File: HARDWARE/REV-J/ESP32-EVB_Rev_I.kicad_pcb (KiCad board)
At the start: 2 copper layers, 75.2 x 74.7 mm, 159 parts, among them CON1 TB3 DG306-5.0-3P, CON2 TB3 DG306-5.0-3P, Q1 BC817-40(SOT23), Q2 BC817-40(SOT23), Q3 Q12MHz/20pF/30ppm/2P/HC-49SM(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, Q4 BC817-40(SOT23), Q5 BC817-40(SOT23), Q6 BC817, Q7 BC817-40(SOT23), U1 BL4054B-42TPRN(SOT23-5), U10 BAT54C(SOT23-3), U2 SY8089AAAC(SOT23-5), U3 ESP-WROOM-32, U4 LAN8710A-EZC(QFN32), U5 CH340T(SSOP20W), U6 MCP2562-E/SN(SOIC-8_150mil), U7 RPM7236-H8, U8 NCP303LSN27T1G(SOT-23-5), U9 BAT54C(SOT23-3)

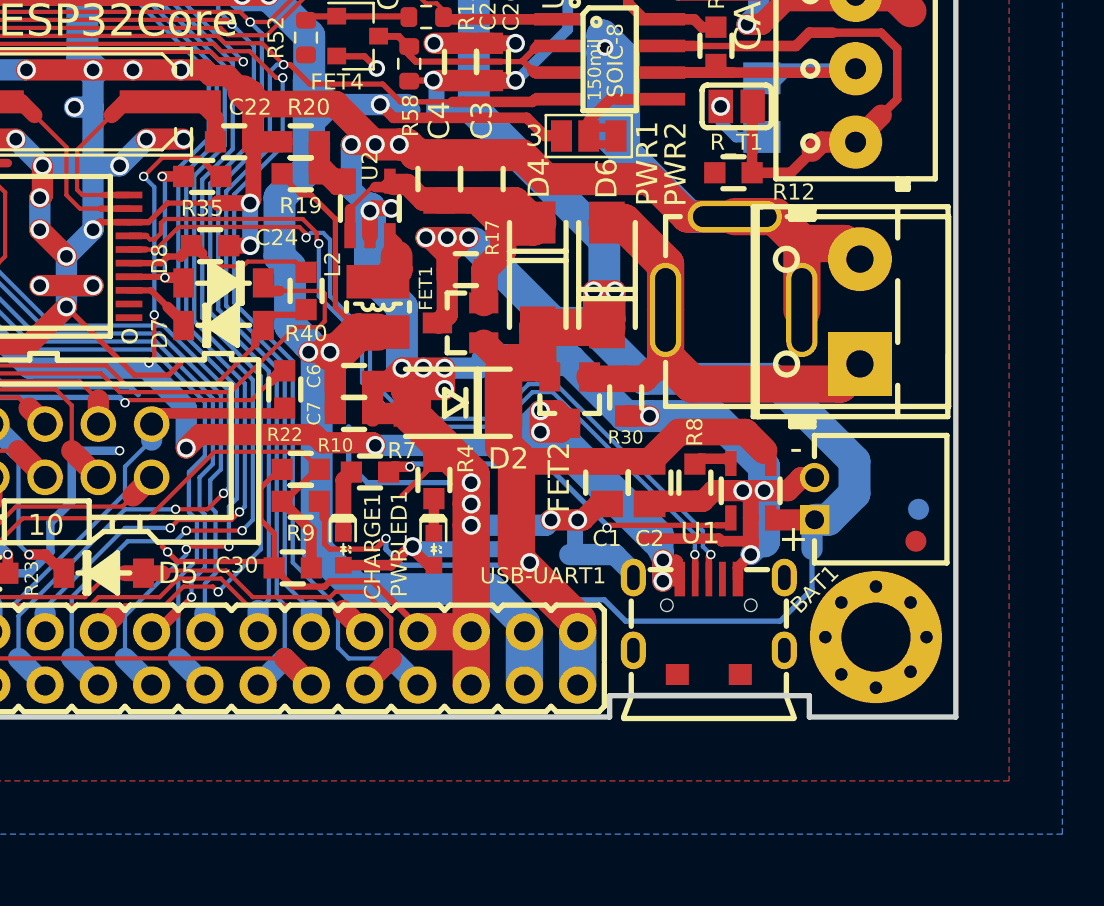
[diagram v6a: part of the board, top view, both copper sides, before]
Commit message: re-position usb port+bat conector
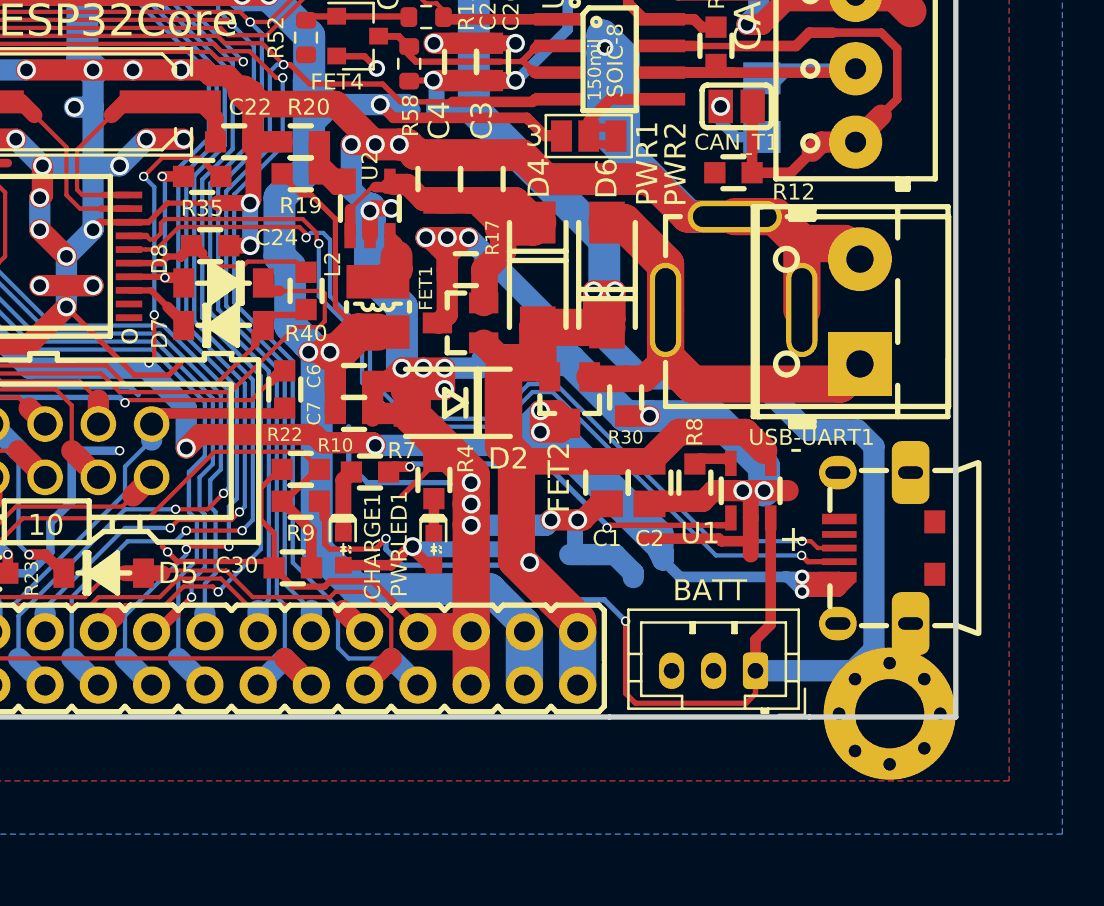
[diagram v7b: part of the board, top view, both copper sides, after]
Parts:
- removed BAT1: DW02R, OLIMEX_Connectors-FP:LIPO_BAT-CON2DW02R
- removed Fid2: , OLIMEX_Other-FP:Fiducial1x3
- removed GND1: TESTPAD, OLIMEX_Other-FP:TESTPAD_40-ROUND
- added BATT: Conn_01x03, Connector_JST:JST_PH_B3B-PH-K_1x03_P2.00mm_Vertical, F.Cu at (135.2, 139.5)
- moved USB-UART1 10.5 mm to (142.4, 133.7), turned to 0 degrees
- moved MH2 3.71 mm to (141.6, 141.6)
- renumbered R_T1 to CAN_T1
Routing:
- net /+5V_USB: track 86.5 -> 101.8 mm
- net Net-(FET1-Pad3): track 73.9 -> 88.7 mm, vias 4 -> 5
- net GND: track 1017.3 -> 1011.1 mm, vias 134 -> 133
- net Net-(U5-Pad7): track 40.4 -> 45.7 mm
- net Net-(U5-Pad6): track 40.8 -> 45.1 mm
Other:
- outline, holes or cut-outs redrawn

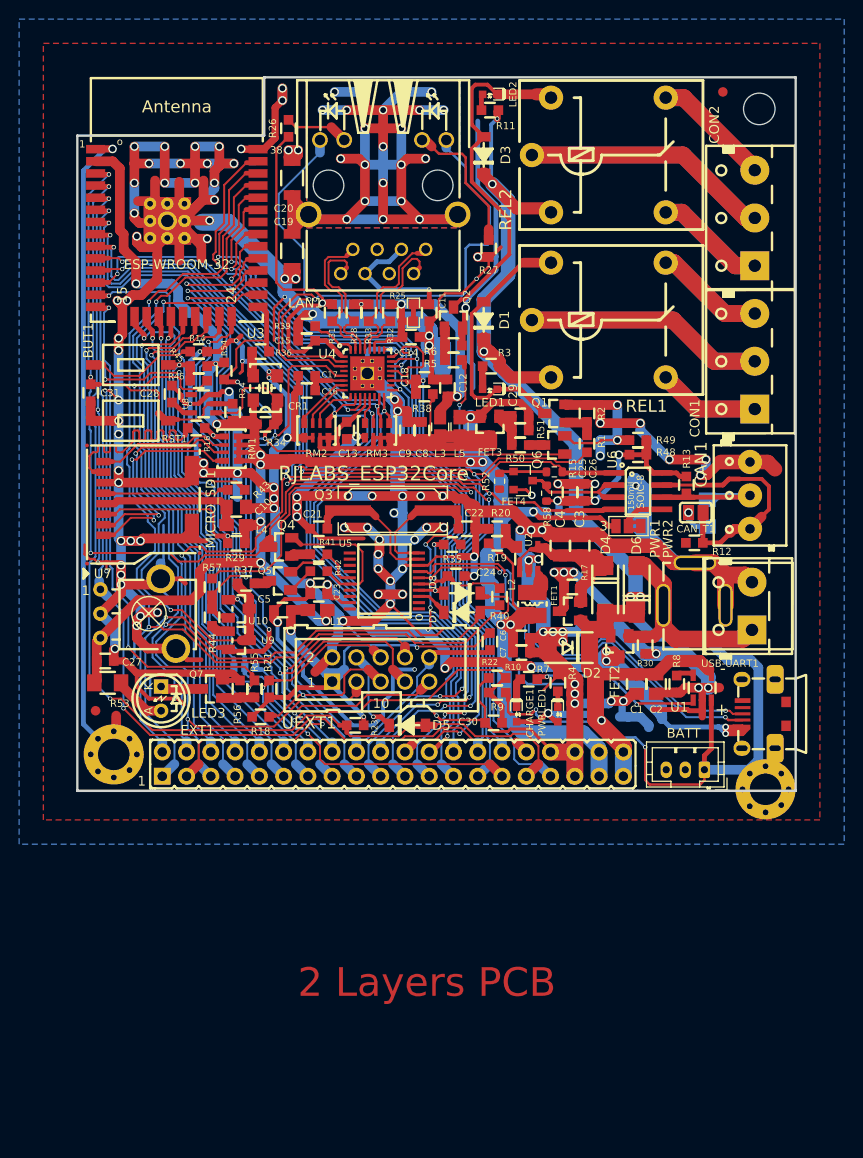
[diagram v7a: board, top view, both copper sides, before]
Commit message: done add 5 extension UEXT
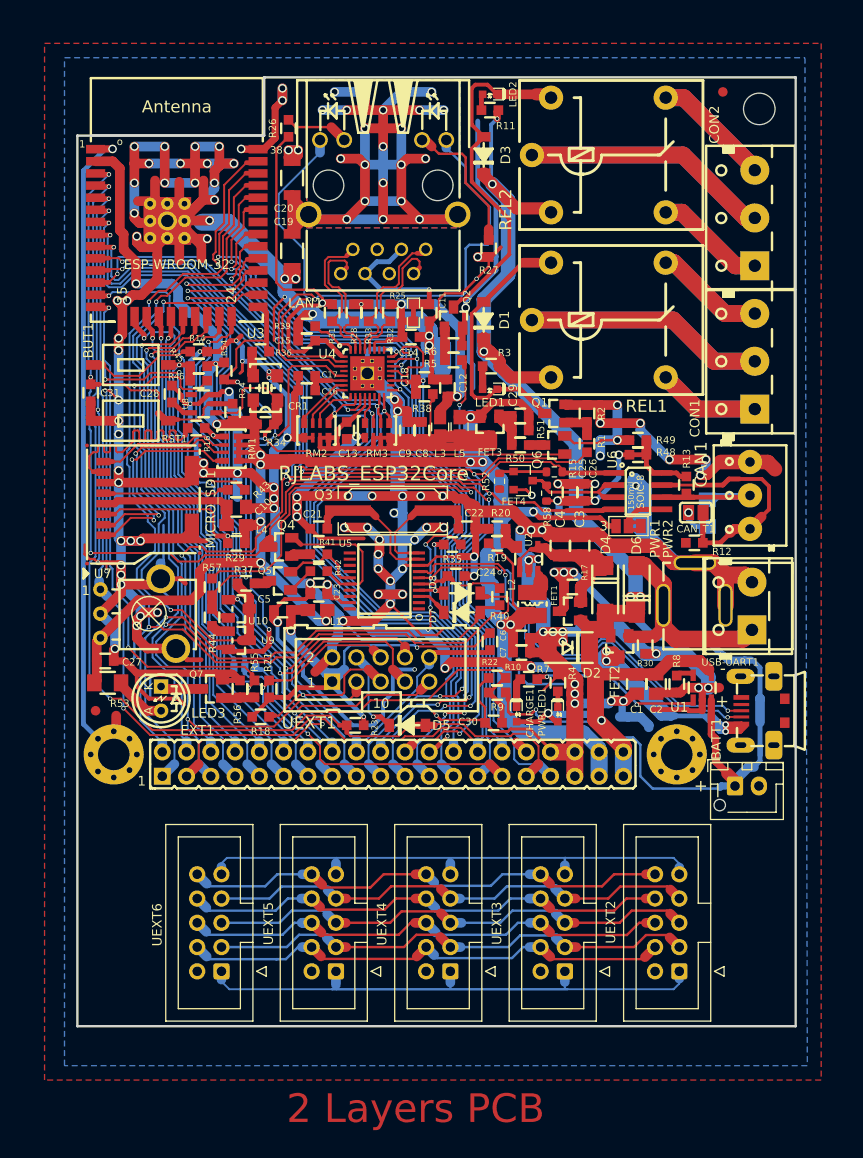
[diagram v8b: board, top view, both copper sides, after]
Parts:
- removed BATT: Conn_01x03, Connector_JST:JST_PH_B3B-PH-K_1x03_P2.00mm_Vertical
- added BATT1: Conn_01x02, Connector_JST:JST_XH_B2B-XH-AM_1x02_P2.50mm_Vertical, F.Cu at (138.4, 141.2)
- added UEXT2: BH10S, Connector_IDC:IDC-Header_2x05_P2.54mm_Vertical, F.Cu at (132.6, 160.6)
- added UEXT3: BH10S, Connector_IDC:IDC-Header_2x05_P2.54mm_Vertical, F.Cu at (120.6, 160.6)
- added UEXT4: BH10S, Connector_IDC:IDC-Header_2x05_P2.54mm_Vertical, F.Cu at (108.6, 160.6)
- added UEXT5: BH10S, Connector_IDC:IDC-Header_2x05_P2.54mm_Vertical, F.Cu at (96.7, 160.6)
- added UEXT6: BH10S, Connector_IDC:IDC-Header_2x05_P2.54mm_Vertical, F.Cu at (84.7, 160.6)
- moved MH2 9.98 mm to (132.3, 137.9)
- moved USB-UART1 0.35 mm to (142.2, 133.3)
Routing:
- net Net-(UEXT2-Pad1): track 0.00 -> 57.8 mm
- net Net-(UEXT2-Pad9): track 0.00 -> 55.9 mm
- net Net-(UEXT2-Pad6): track 0.00 -> 53.1 mm
- net Net-(UEXT2-Pad4): track 0.00 -> 52.4 mm
- net Net-(UEXT2-Pad7): track 0.00 -> 52.3 mm
- net Net-(UEXT2-Pad10): track 0.00 -> 52.2 mm
- net Net-(UEXT2-Pad3): track 0.00 -> 52.1 mm
- net Net-(UEXT2-Pad5): track 0.00 -> 52.1 mm
- net Net-(UEXT2-Pad8): track 0.00 -> 52.0 mm
- net /+5V_USB: track 101.8 -> 111.8 mm
- net Net-(BATT1-Pad1): track 88.7 -> 97.4 mm, vias 5 -> 4
- net GND: track 1011.1 -> 1010.4 mm
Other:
- board size 75.2 x 74.7 mm -> 75.2 x 99.3 mm
